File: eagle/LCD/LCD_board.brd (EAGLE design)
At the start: 160 x 100 mm, 7 parts, among them CN1 1X4-CLEANBIG

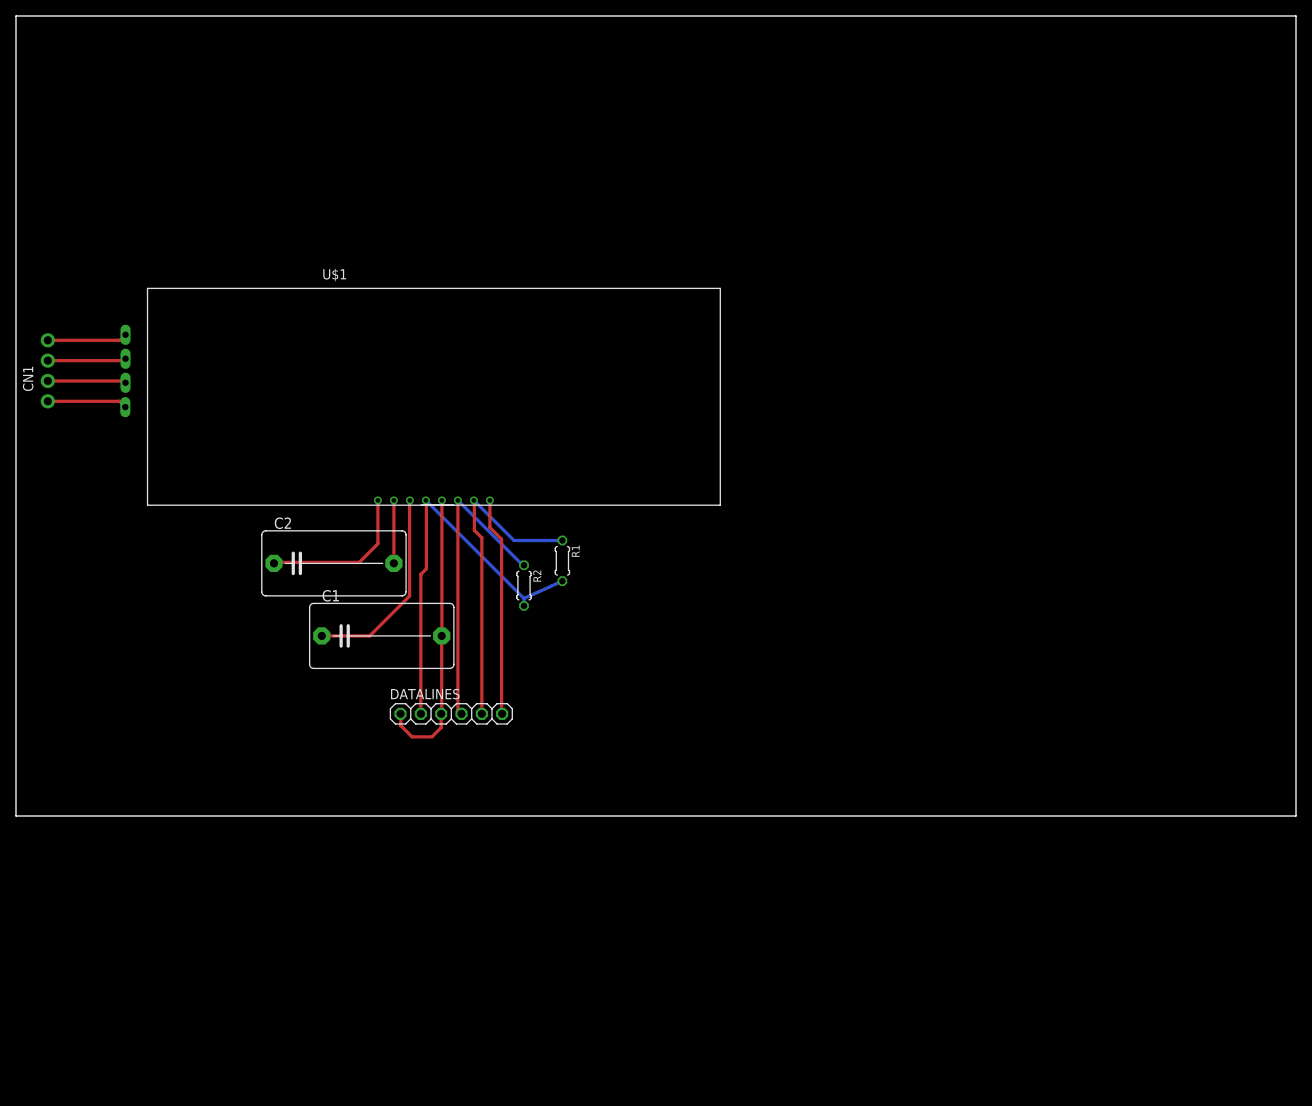
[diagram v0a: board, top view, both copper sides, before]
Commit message: Updated LCD_board.sch with modified LCD screen schematic.
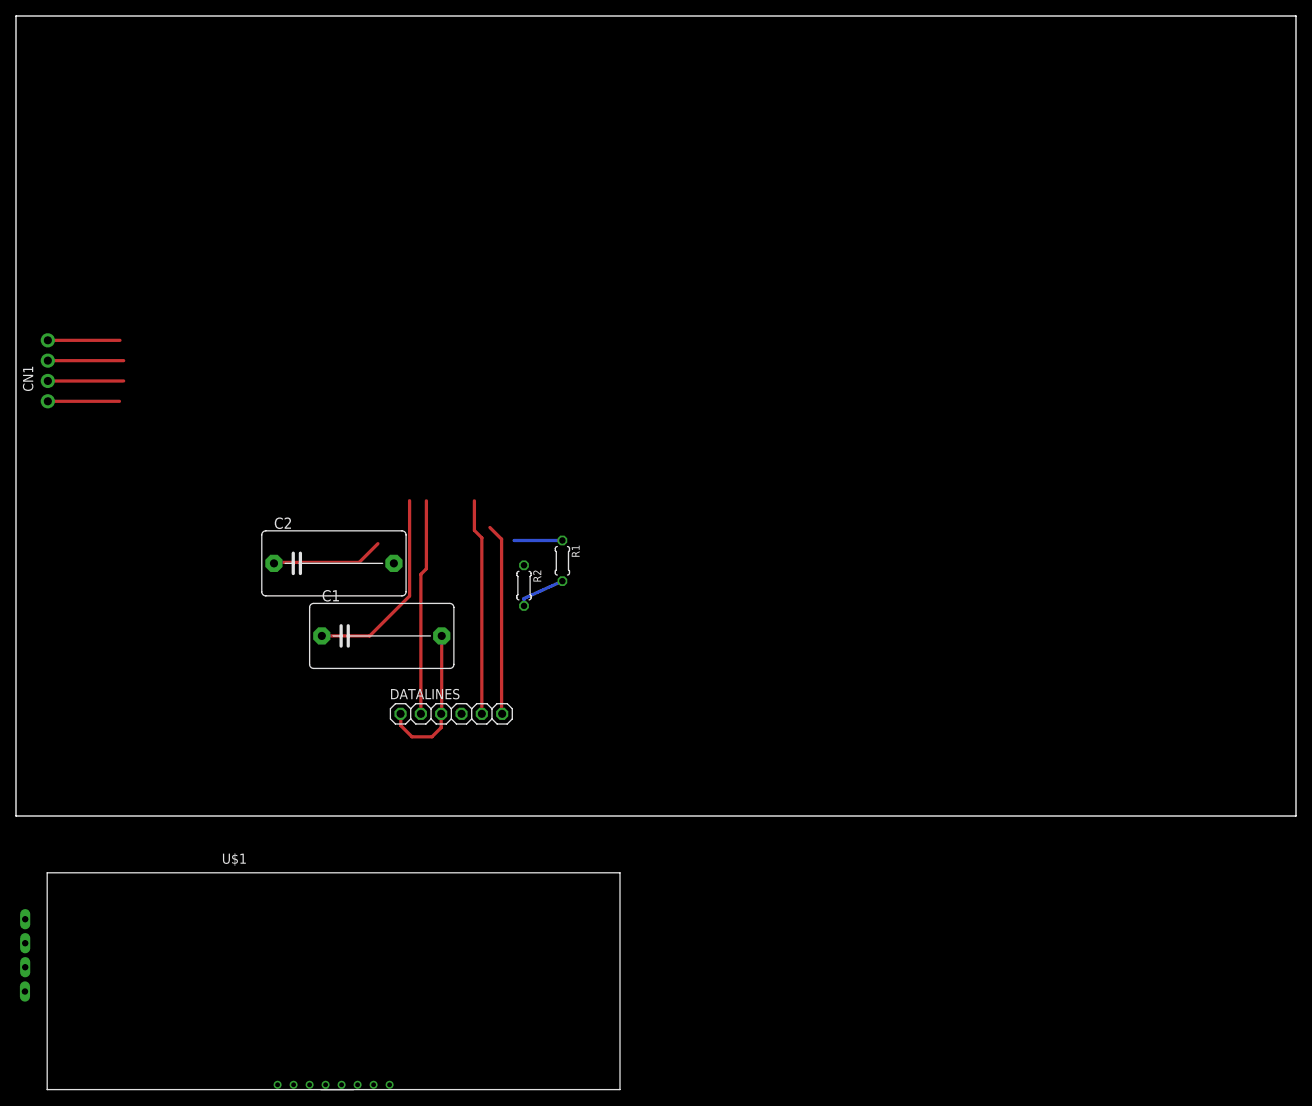
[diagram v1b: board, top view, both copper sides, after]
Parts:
- U$1: value NHD-C0220BIZ-FS(RGB)-FBW-3VM -> NHD-C0220BIZ
- moved U$1 74.1 mm to (39.7, -17.4)
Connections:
- net GND: no longer U$1.P$4
- net N$3: now also U$1.P$4
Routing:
- net SDA: track 38.5 -> 0.79 mm
- net VDD: track 50.5 -> 33.1 mm
- net GND: track 36.0 -> 19.1 mm
- net C1+: track 7.87 -> 0.01 mm
- net SCL: track 40.2 -> 33.1 mm
- net N$1: track 19.4 -> 14.0 mm
- net RST: track 27.3 -> 23.9 mm
- net N$4: track 9.98 -> 8.95 mm
- net A: track 10.00 -> 9.02 mm
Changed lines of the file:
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@@
 </autorouter>
 <elements>
-<element name="U$1" library="LockBox" package="NHD-C0220BIZ-LCD" value="NHD-C0220BIZ-FS(RGB)-FBW-3VM" x="52.24" y="55.65">
-<attribute name="COG" value="2x20" x="105.58" y="37.87" size="1.778" layer="27" display="off"/>
-<attribute name="INTERFACE" value="I2C" x="105.58" y="37.87" size="1.778" layer="27" display="off"/>
-<attribute name="VOLTS" value="3.3V" x="105.58" y="37.87" size="1.778" layer="27" display="off"/>
-</element>
 <element name="DATALINES" library="adafruit" package="1X06" value="To MPU" x="54.42" y="12.77">
 <attribute name="DATALINES" value="" x="114.11" y="-26.6" size="1.778" layer="27" display="off"/>
@@
 <element name="R1" library="LockBox" package="0204/5" value="4.7k" x="68.3" y="31.9" rot="R270"/>
 <element name="R2" library="LockBox" package="0204/5" value="4.7k" x="63.5" y="28.8" rot="R270"/>
+<element name="U$1" library="LockBox" package="NHD-C0220BIZ-LCD" value="NHD-C0220BIZ" x="39.7" y="-17.4">
+<attribute name="COG" value="2x20" x="39.7" y="-17.4" size="1.778" layer="27" display="off"/>
+<attribute name="INTERFACE" value="I2C" x="39.7" y="-17.4" size="1.778" layer="27" display="off"/>
+<attribute name="VOLTS" value="3.3V" x="39.7" y="-17.4" size="1.778" layer="27" display="off"/>
+</element>
 </elements>
 <signals>
 <signal name="N$1">
-<contactref element="U$1" pad="P$8"/>
 <contactref element="C2" pad="1"/>
-<wire x1="45.24" y1="39.45" x2="45.24" y2="34.04" width="0.4064" layer="1"/>
 <wire x1="45.24" y1="34.04" x2="42.9" y2="31.7" width="0.4064" layer="1"/>
 <wire x1="42.9" y1="31.7" x2="32.367" y2="31.7" width="0.4064" layer="1"/>
 <wire x1="32.367" y1="31.7" x2="32.247" y2="31.58" width="0.4064" layer="1"/>
+<contactref element="U$1" pad="P$8"/>
+<wire x1="32.7" y1="-33.6" x2="32.247" y2="31.58" width="0" layer="19" extent="1-1"/>
 </signal>
 <signal name="C1+">
 <contactref element="C2" pad="2"/>
+<wire x1="47.24" y1="31.587" x2="47.233" y2="31.58" width="0.4064" layer="1"/>
 <contactref element="U$1" pad="P$7"/>
-<wire x1="47.24" y1="39.45" x2="47.24" y2="31.587" width="0.4064" layer="1"/>
-<wire x1="47.24" y1="31.587" x2="47.233" y2="31.58" width="0.4064" layer="1"/>
+<wire x1="34.7" y1="-33.6" x2="47.233" y2="31.58" width="0" layer="19" extent="1-1"/>
 </signal>
 <signal name="N$3">
-<contactref element="U$1" pad="P$6"/>
 <contactref element="C1" pad="1"/>
 <wire x1="38.227" y1="22.51" x2="44.21" y2="22.51" width="0.4064" layer="1"/>
 <wire x1="44.21" y1="22.51" x2="49.2" y2="27.5" width="0.4064" layer="1"/>
 <wire x1="49.2" y1="27.5" x2="49.2" y2="39.41" width="0.4064" layer="1"/>
-<wire x1="49.2" y1="39.41" x2="49.24" y2="39.45" width="0.4064" layer="1"/>
+<contactref element="U$1" pad="P$4"/>
+<contactref element="U$1" pad="P$6"/>
+<wire x1="36.7" y1="-33.6" x2="38.227" y2="22.51" width="0" layer="19" extent="1-1"/>
+<wire x1="40.7" y1="-33.6" x2="36.7" y2="-33.6" width="0" layer="19" extent="1-1"/>
 </signal>
 <signal name="RST">
-<contactref element="U$1" pad="P$1"/>
 <contactref element="DATALINES" pad="6"/>
-<wire x1="59.24" y1="39.45" x2="59.24" y2="36.06" width="0.4064" layer="1"/>
 <wire x1="59.24" y1="36.06" x2="60.7" y2="34.6" width="0.4064" layer="1"/>
 <wire x1="60.7" y1="34.6" x2="60.7" y2="12.84" width="0.4064" layer="1"/>
 <wire x1="60.7" y1="12.84" x2="60.77" y2="12.77" width="0.4064" layer="1"/>
+<contactref element="U$1" pad="P$1"/>
+<wire x1="46.7" y1="-33.6" x2="60.77" y2="12.77" width="0" layer="19" extent="1-1"/>
 </signal>
 <signal name="SCL">
 <contactref element="DATALINES" pad="5"/>
-<contactref element="U$1" pad="P$2"/>
 <wire x1="58.23" y1="12.77" x2="58.23" y2="34.77" width="0.4064" layer="1"/>
 <wire x1="58.23" y1="34.77" x2="57.3" y2="35.7" width="0.4064" layer="1"/>
 <wire x1="57.3" y1="35.7" x2="57.3" y2="39.39" width="0.4064" layer="1"/>
-<wire x1="57.3" y1="39.39" x2="57.24" y2="39.45" width="0.4064" layer="1"/>
 <contactref element="R1" pad="1"/>
 <wire x1="68.3" y1="34.44" x2="62.25" y2="34.44" width="0.4064" layer="16"/>
-<wire x1="62.25" y1="34.44" x2="57.24" y2="39.45" width="0.4064" layer="16"/>
+<contactref element="U$1" pad="P$2"/>
+<wire x1="58.23" y1="34.77" x2="62.25" y2="34.44" width="0" layer="19" extent="1-16"/>
+<wire x1="44.7" y1="-33.6" x2="58.23" y2="12.77" width="0" layer="19" extent="1-1"/>
 </signal>
 <signal name="SDA">
 <contactref element="DATALINES" pad="4"/>
-<contactref element="U$1" pad="P$3"/>
-<wire x1="55.24" y1="39.45" x2="55.24" y2="13.22" width="0.4064" layer="1"/>
 <wire x1="55.24" y1="13.22" x2="55.69" y2="12.77" width="0.4064" layer="1"/>
 <contactref element="R2" pad="1"/>
 <wire x1="63.5" y1="31.34" x2="63.35" y2="31.34" width="0.4064" layer="16"/>
-<wire x1="63.35" y1="31.34" x2="55.24" y2="39.45" width="0.4064" layer="16"/>
+<contactref element="U$1" pad="P$3"/>
+<wire x1="55.24" y1="13.22" x2="63.35" y2="31.34" width="0" layer="19" extent="1-16"/>
+<wire x1="42.7" y1="-33.6" x2="55.69" y2="12.77" width="0" layer="19" extent="1-1"/>
 </signal>
 <signal name="VDD">
 <contactref element="DATALINES" pad="2"/>
-<contactref element="U$1" pad="P$5"/>
 <wire x1="50.61" y1="12.77" x2="50.61" y2="30.21" width="0.4064" layer="1"/>
 <wire x1="50.61" y1="30.21" x2="51.3" y2="30.9" width="0.4064" layer="1"/>
 <wire x1="51.3" y1="30.9" x2="51.3" y2="39.39" width="0.4064" layer="1"/>
-<wire x1="51.3" y1="39.39" x2="51.24" y2="39.45" width="0.4064" layer="1"/>
 <contactref element="R1" pad="2"/>
 <contactref element="R2" pad="2"/>
 <wire x1="63.5" y1="26.26" x2="63.5" y2="27.19" width="0.4064" layer="16"/>
-<wire x1="63.5" y1="27.19" x2="51.24" y2="39.45" width="0.4064" layer="16"/>
 <wire x1="63.5" y1="27.19" x2="68.3" y2="29.36" width="0.4064" layer="16"/>
+<contactref element="U$1" pad="P$5"/>
+<wire x1="51.3" y1="30.9" x2="63.5" y2="27.19" width="0" layer="19" extent="1-16"/>
+<wire x1="38.7" y1="-33.6" x2="50.61" y2="12.77" width="0" layer="19" extent="1-1"/>
 </signal>
 <signal name="GND">
 <contactref element="DATALINES" pad="1"/>
-<contactref element="U$1" pad="P$4"/>
 <contactref element="DATALINES" pad="3"/>
 <contactref element="C1" pad="2"/>
-<wire x1="53.24" y1="39.45" x2="53.24" y2="22.537" width="0.4064" layer="1"/>
 <wire x1="53.24" y1="22.537" x2="53.213" y2="22.51" width="0.4064" layer="1"/>
 <wire x1="53.213" y1="22.51" x2="53.213" y2="12.833" width="0.4064" layer="1"/>
@@
 </signal>
 <signal name="A">
-<contactref element="U$1" pad="P$RK"/>
 <contactref element="CN1" pad="4"/>
 <wire x1="3.98" y1="59.46" x2="13" y2="59.46" width="0.4064" layer="1"/>
-<wire x1="13" y1="59.46" x2="13.69" y2="60.15" width="0.4064" layer="1"/>
+<contactref element="U$1" pad="P$RK"/>
+<wire x1="1.15" y1="-12.9" x2="3.98" y2="59.46" width="0" layer="19" extent="1-1"/>
 </signal>
 <signal name="GK">
-<contactref element="U$1" pad="P$BK"/>
 <contactref element="CN1" pad="2"/>
 <wire x1="3.98" y1="54.38" x2="13.46" y2="54.38" width="0.4064" layer="1"/>
-<wire x1="13.46" y1="54.38" x2="13.69" y2="54.15" width="0.4064" layer="1"/>
+<contactref element="U$1" pad="P$BK"/>
+<wire x1="1.15" y1="-18.9" x2="3.98" y2="54.38" width="0" layer="19" extent="1-1"/>
 </signal>
 <signal name="N$2">
-<contactref element="U$1" pad="P$GK"/>
 <contactref element="CN1" pad="3"/>
 <wire x1="3.98" y1="56.92" x2="13.46" y2="56.92" width="0.4064" layer="1"/>
-<wire x1="13.46" y1="56.92" x2="13.69" y2="57.15" width="0.4064" layer="1"/>
+<contactref element="U$1" pad="P$GK"/>
+<wire x1="1.15" y1="-15.9" x2="3.98" y2="56.92" width="0" layer="19" extent="1-1"/>
 </signal>
 <signal name="N$4">
 <contactref element="CN1" pad="1"/>
+<wire x1="3.98" y1="51.84" x2="12.93" y2="51.84" width="0.4064" layer="1"/>
 <contactref element="U$1" pad="P$A"/>
-<wire x1="3.98" y1="51.84" x2="12.93" y2="51.84" width="0.4064" layer="1"/>
-<wire x1="12.93" y1="51.84" x2="13.66" y2="51.11" width="0.4064" layer="1"/>
+<wire x1="1.12" y1="-21.94" x2="3.98" y2="51.84" width="0" layer="19" extent="1-1"/>
 </signal>
 </signals>

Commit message: LCD_board.brd is now a one layer board.  Created new Gerber files and updated the GerberFiles/LCD directory with these new files
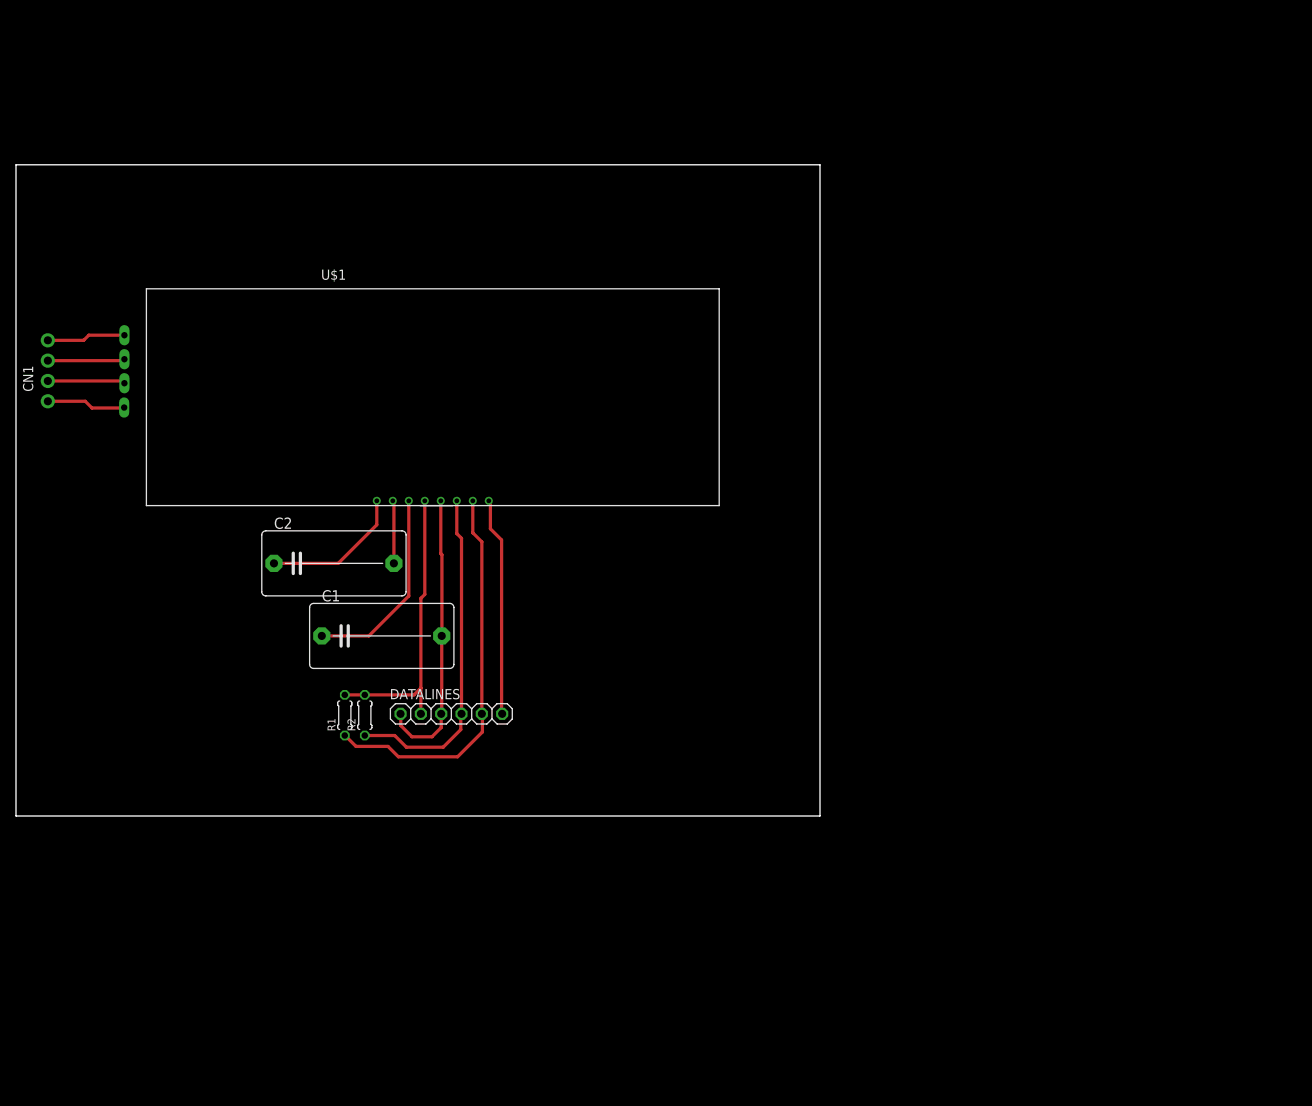
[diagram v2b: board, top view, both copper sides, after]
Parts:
- moved U$1 74.0 mm to (52.1, 55.6)
- moved R1 33.4 mm to (41.1, 12.6), turned to 90 degrees
- moved R2 25.7 mm to (43.6, 12.6), turned to 90 degrees
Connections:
- removed net N$3: C1.1, U$1.P$4, U$1.P$6
- new net N$5: C1.1, U$1.P$6
- net GND: now also U$1.P$4
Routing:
- net SDA: track 0.79 -> 42.4 mm
- net N$3: track 24.9 -> 0.00 mm
- net N$5: track 0.00 -> 24.8 mm
- net GND: track 19.1 -> 36.0 mm
- net SCL: track 33.1 -> 49.0 mm
- net C1+: track 0.01 -> 7.87 mm
- net N$1: track 14.0 -> 17.8 mm
- net VDD: track 33.1 -> 36.7 mm
- net RST: track 23.9 -> 27.3 mm
- net N$4: track 8.95 -> 9.91 mm
- net A: track 9.02 -> 9.84 mm
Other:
- board size 160 x 100 mm -> 100.5 x 81.4 mm
